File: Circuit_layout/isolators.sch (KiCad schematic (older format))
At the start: 28 parts, among them U16 MCP6004, U17 ACPL-C870, U18 ACPL-C870

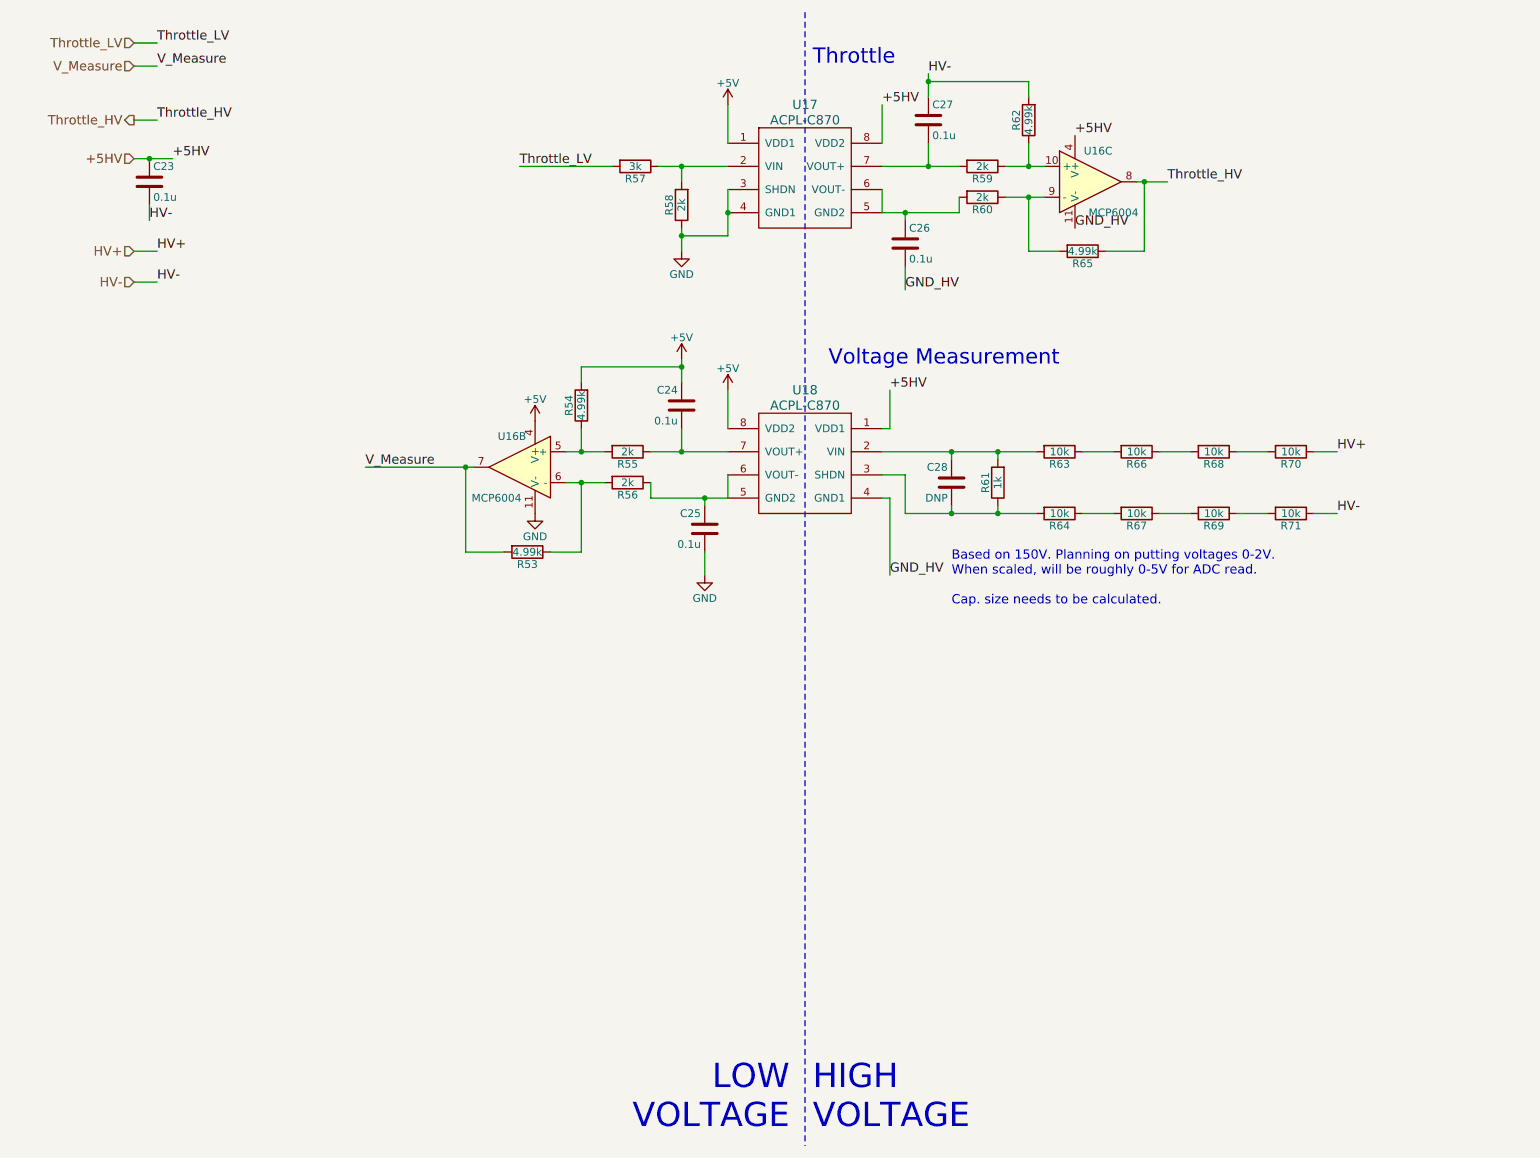
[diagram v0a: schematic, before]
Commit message: finished adding footprints/info to all parts that I can
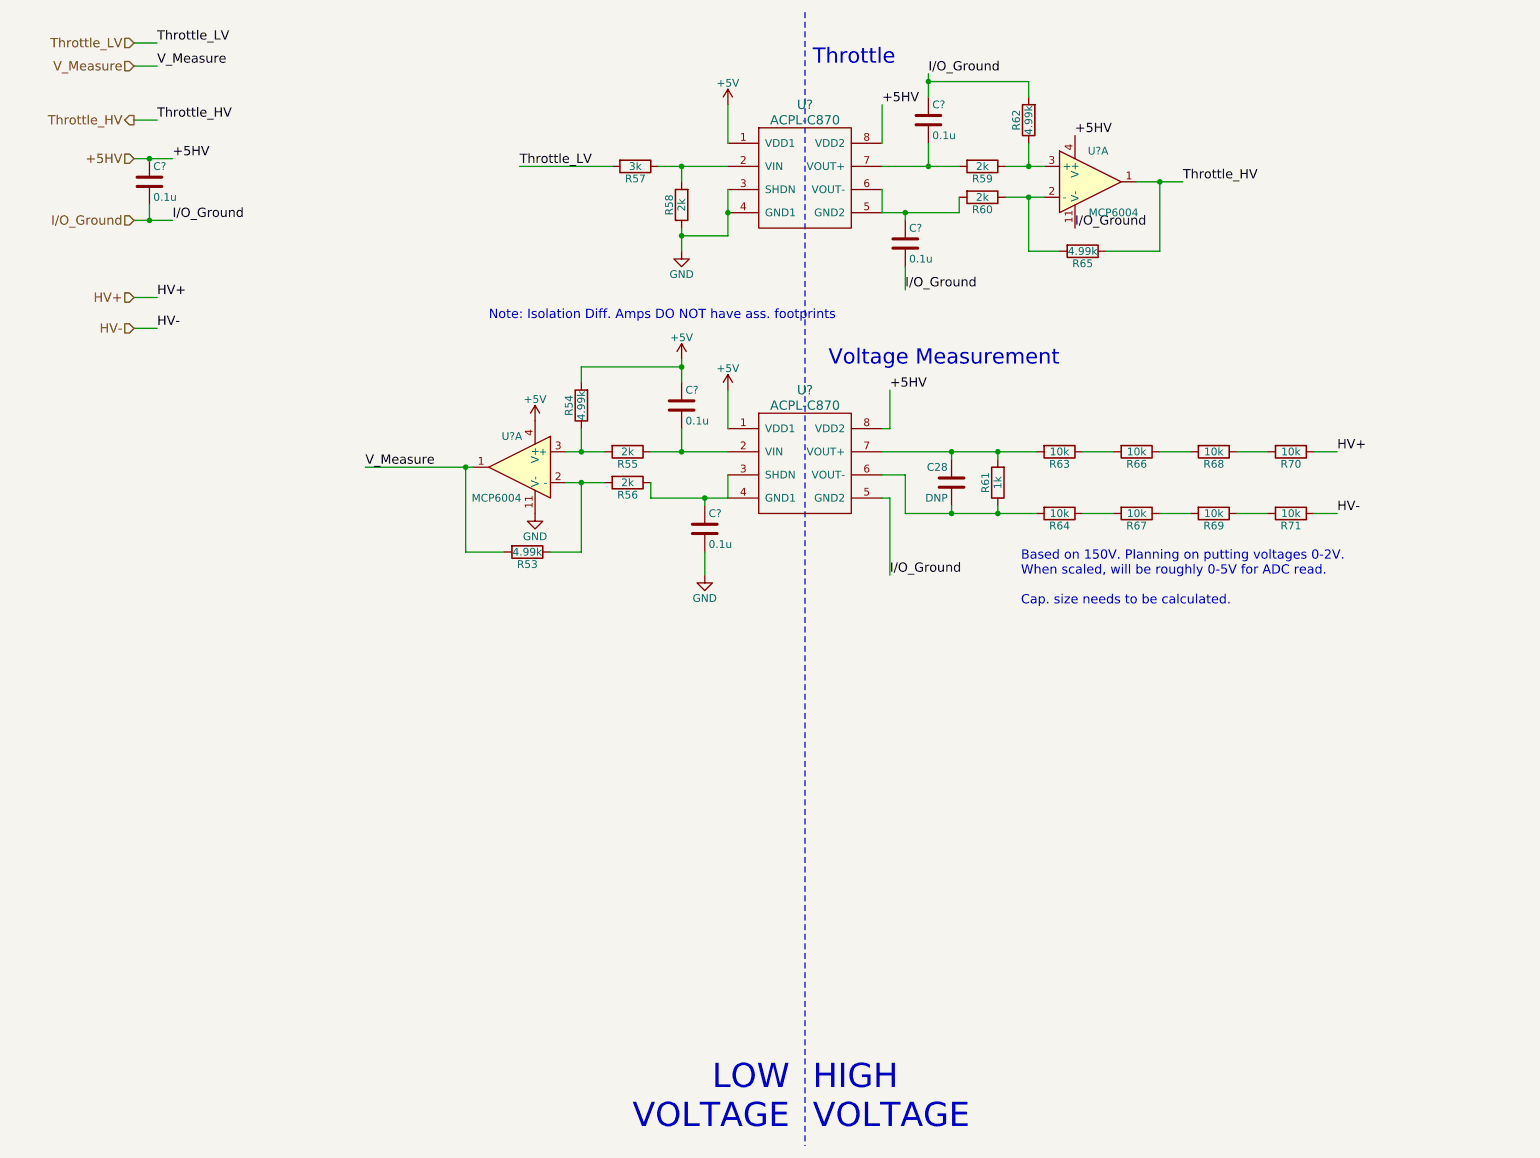
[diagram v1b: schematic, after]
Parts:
- removed C23, C24, C25, C26, C27: 0.1u, symbol C
- removed U16: MCP6004, symbol MCP6004
- removed U17, U18: ACPL-C870, symbol ACPL-C870
- added C? (x5): 0.1u, Capacitors_SMD:C_0805_HandSoldering, symbol C
- added U? (x2): ACPL-C870, symbol ACPL-C870
- added U? (x2): MCP6004, Housings_SOIC:SOIC-14_3.9x8.7mm_Pitch1.27mm, symbol MCP6004
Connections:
- net +5HV: now also C?.1, U?.4 (V+), U?.8 (VDD2), U?.8 (VDD2)
- net +5V: now also C?.1, U?.1 (VDD1), U?.1 (VDD1), U?.4 (V+)
- net GND: now also C?.2, U?.11 (V-), U?.3 (SHDN), U?.4 (GND1)
- net HV-: no longer R62.2
- net Throttle_HV: now also U?.1
- net V_Measure: now also U?.1
- net at R57.1, R58.2: now also U?.2 (VIN)
- net at R60.2: now also C?.1, U?.5 (GND2), U?.6 (VOUT-)
- net at R59.2: now also C?.2, U?.7 (VOUT+)
- net at R59.1, R62.1: now also U?.3 (+)
- net at R60.1, R65.2: now also U?.2 (-)
- net at C28.1, R61.2, R63.2: now also U?.7 (VOUT+)
- net at C28.2, R61.1, R64.2: now also U?.6 (VOUT-)
- net at R56.1: now also C?.1, U?.3 (SHDN), U?.4 (GND1)
- net at R55.1: now also C?.2, U?.2 (VIN)
- net at R54.1, R55.2: now also U?.3 (+)
- net at R53.1, R56.2: now also U?.2 (-)
- new net I/O_Ground: C?.1, C?.2, C?.2, R62.2, U?.11 (V-), U?.5 (GND2)
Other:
- note added: "Note: Isolation Diff. Amps DO NOT have ass. footprints"

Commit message: took notes w/ greg
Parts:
- gave numbers to parts that had none: 8
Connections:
- net Throttle_HV: now also U17.14; no longer U17.1
- net V_Measure: now also U17.8; no longer U17.1
- net at R60.1, R65.2: now also U17.13 (-); no longer U17.2 (-)
- net at R59.1, R62.1: now also U17.12 (+); no longer U17.3 (+)
- net at R53.1, R56.2: now also U17.9 (-); no longer U17.2 (-)
- net at R54.1, R55.2: now also U17.10 (+); no longer U17.3 (+)
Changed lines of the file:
@@
 	3250 3950 3500 3950
 $Comp
-L +5V #PWR088
+L +5V #PWR087
 U 1 1 58B246C4
 P 4650 2700
-F 0 "#PWR088" H 4650 2550 50  0001 C CNN
+F 0 "#PWR087" H 4650 2550 50  0001 C CNN
 F 1 "+5V" H 4650 2840 50  0000 C CNN
 F 2 "" H 4650 2700 50  0000 C CNN
@@
 $EndComp
 $Comp
-L +5V #PWR089
+L +5V #PWR088
 U 1 1 58B24710
 P 4950 2900
-F 0 "#PWR089" H 4950 2750 50  0001 C CNN
+F 0 "#PWR088" H 4950 2750 50  0001 C CNN
 F 1 "+5V" H 4950 3040 50  0000 C CNN
 F 2 "" H 4950 2900 50  0000 C CNN
@@
 $EndComp
 $Comp
-L +5V #PWR090
+L +5V #PWR089
 U 1 1 58B2475C
 P 3700 3100
-F 0 "#PWR090" H 3700 2950 50  0001 C CNN
+F 0 "#PWR089" H 3700 2950 50  0001 C CNN
 F 1 "+5V" H 3700 3240 50  0000 C CNN
 F 2 "" H 3700 3100 50  0000 C CNN
@@
 $EndComp
 $Comp
-L GND #PWR091
+L GND #PWR090
 U 1 1 58B247A8
 P 3700 3700
-F 0 "#PWR091" H 3700 3450 50  0001 C CNN
+F 0 "#PWR090" H 3700 3450 50  0001 C CNN
 F 1 "GND" H 3700 3550 50  0000 C CNN
 F 2 "" H 3700 3700 50  0000 C CNN
@@
 $EndComp
 $Comp
-L GND #PWR092
+L GND #PWR091
 U 1 1 58B2480E
 P 4800 4100
-F 0 "#PWR092" H 4800 3850 50  0001 C CNN
+F 0 "#PWR091" H 4800 3850 50  0001 C CNN
 F 1 "GND" H 4800 3950 50  0000 C CNN
 F 2 "" H 4800 4100 50  0000 C CNN
@@
 	4950 1900 4650 1900
 $Comp
-L GND #PWR093
+L GND #PWR092
 U 1 1 58B25770
 P 4650 2000
-F 0 "#PWR093" H 4650 1750 50  0001 C CNN
+F 0 "#PWR092" H 4650 1750 50  0001 C CNN
 F 1 "GND" H 4650 1850 50  0000 C CNN
 F 2 "" H 4650 2000 50  0000 C CNN
@@
 $EndComp
 $Comp
-L +5V #PWR094
+L +5V #PWR093
 U 1 1 58B257CF
 P 4950 1050
-F 0 "#PWR094" H 4950 900 50  0001 C CNN
+F 0 "#PWR093" H 4950 900 50  0001 C CNN
 F 1 "+5V" H 4950 1190 50  0000 C CNN
 F 2 "" H 4950 1050 50  0000 C CNN
@@
 $EndComp
 $Comp
-L C C?
+L C C25
 U 1 1 58B44F65
 P 1200 1550
-F 0 "C?" H 1225 1650 50  0000 L CNN
+F 0 "C25" H 1225 1650 50  0000 L CNN
 F 1 "0.1u" H 1225 1450 50  0000 L CNN
 F 2 "Capacitors_SMD:C_0805_HandSoldering" H 1238 1400 50  0001 C CNN
@@
 $EndComp
 $Comp
-L ACPL-C870 U?
+L ACPL-C870 U19
 U 1 1 58B45431
 P 5450 1250
-F 0 "U?" H 5450 1450 60  0000 C CNN
+F 0 "U19" H 5450 1450 60  0000 C CNN
 F 1 "ACPL-C870" H 5450 1350 60  0000 C CNN
 F 2 "" H 5450 1450 60  0000 C CNN
@@
 Note: Isolation Diff. Amps DO NOT have ass. footprints
 $Comp
-L ACPL-C870 U?
+L ACPL-C870 U20
 U 1 1 58B35F2C
 P 5450 3100
-F 0 "U?" H 5450 3300 60  0000 C CNN
+F 0 "U20" H 5450 3300 60  0000 C CNN
 F 1 "ACPL-C870" H 5450 3200 60  0000 C CNN
 F 2 "" H 5450 3300 60  0000 C CNN
@@
 $EndComp
 $Comp
-L C C?
+L C C26
 U 1 1 58B362A1
 P 4650 3000
-F 0 "C?" H 4675 3100 50  0000 L CNN
+F 0 "C26" H 4675 3100 50  0000 L CNN
 F 1 "0.1u" H 4675 2900 50  0000 L CNN
 F 2 "Capacitors_SMD:C_0805_HandSoldering" H 4688 2850 50  0001 C CNN
@@
 $EndComp
 $Comp
-L C C?
+L C C27
 U 1 1 58B36392
 P 4800 3800
-F 0 "C?" H 4825 3900 50  0000 L CNN
+F 0 "C27" H 4825 3900 50  0000 L CNN
 F 1 "0.1u" H 4825 3700 50  0000 L CNN
 F 2 "Capacitors_SMD:C_0805_HandSoldering" H 4838 3650 50  0001 C CNN
@@
 $EndComp
 $Comp
-L C C?
+L C C30
 U 1 1 58B3649B
 P 6250 1150
-F 0 "C?" H 6275 1250 50  0000 L CNN
+F 0 "C30" H 6275 1250 50  0000 L CNN
 F 1 "0.1u" H 6275 1050 50  0000 L CNN
 F 2 "Capacitors_SMD:C_0805_HandSoldering" H 6288 1000 50  0001 C CNN
@@
 $EndComp
 $Comp
-L C C?
+L C C29
 U 1 1 58B36598
 P 6100 1950
-F 0 "C?" H 6125 2050 50  0000 L CNN
+F 0 "C29" H 6125 2050 50  0000 L CNN
 F 1 "0.1u" H 6125 1850 50  0000 L CNN
 F 2 "Capacitors_SMD:C_0805_HandSoldering" H 6138 1800 50  0001 C CNN
@@
 $EndComp
 $Comp
-L MCP6004 U?
-U 1 1 58B3670F
+L MCP6004 U17
+U 4 1 58B3670F
 P 7300 1550
-F 0 "U?" H 7350 1750 50  0000 C CNN
+F 0 "U17" H 7350 1750 50  0000 C CNN
 F 1 "MCP6004" H 7450 1350 50  0000 C CNN
 F 2 "Housings_SOIC:SOIC-14_3.9x8.7mm_Pitch1.27mm" H 7250 1650 50  0001 C CNN
@@
 F 5 "http://www.digikey.com/product-detail/en/microchip-technology/MCP6004T-I-SL/MCP6004T-I-SLCT-ND/5013527" H 7300 1550 60  0001 C CNN "URL"
 F 6 "MCP6004T-I/SL" H 7300 1550 60  0001 C CNN "Man P/N"
-	1    7300 1550
-	1    0    0    -1
-$EndComp
-$Comp
-L MCP6004 U?
-U 1 1 58B367EC
+	4    7300 1550
+	1    0    0    -1
+$EndComp
+$Comp
+L MCP6004 U17
+U 3 1 58B367EC
 P 3600 3400
-F 0 "U?" H 3650 3600 50  0000 C CNN
+F 0 "U17" H 3650 3600 50  0000 C CNN
 F 1 "MCP6004" H 3750 3200 50  0000 C CNN
 F 2 "Housings_SOIC:SOIC-14_3.9x8.7mm_Pitch1.27mm" H 3550 3500 50  0001 C CNN
@@
 F 5 "http://www.digikey.com/product-detail/en/microchip-technology/MCP6004T-I-SL/MCP6004T-I-SLCT-ND/5013527" H 3600 3400 60  0001 C CNN "URL"
 F 6 "MCP6004T-I/SL" H 3600 3400 60  0001 C CNN "Man P/N"
-	1    3600 3400
+	3    3600 3400
 	-1   0    0    -1
 $EndComp

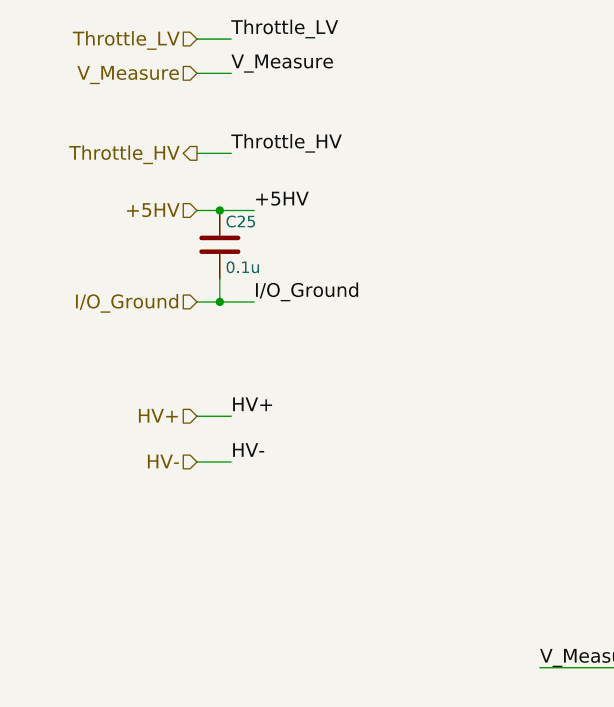
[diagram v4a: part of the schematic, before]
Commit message: got rid of some warnings with nets.
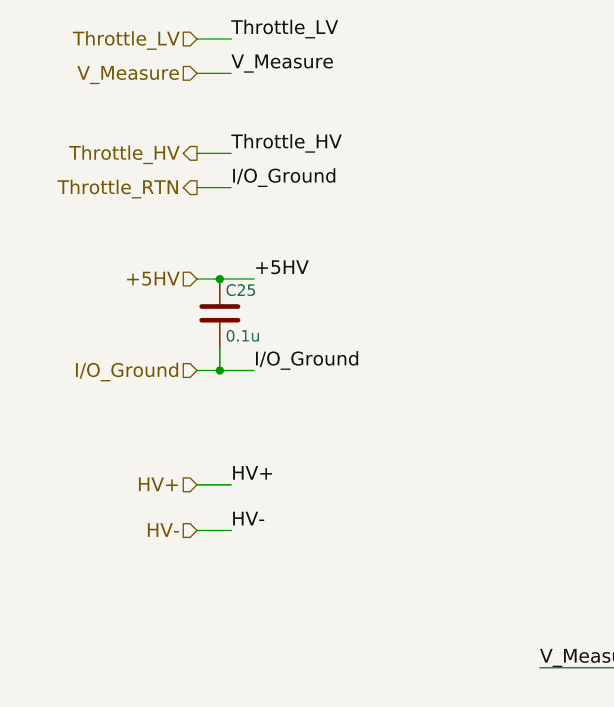
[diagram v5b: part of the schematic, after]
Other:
- moved on the sheet: C25
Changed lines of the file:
@@
 Text HLabel 1100 650  0    60   Input ~ 0
 Throttle_LV
-Text HLabel 1100 1400 0    60   Input ~ 0
+Text HLabel 1100 1700 0    60   Input ~ 0
 +5HV
-Text HLabel 1100 2300 0    60   Input ~ 0
+Text HLabel 1100 2600 0    60   Input ~ 0
 HV+
-Text HLabel 1100 2500 0    60   Input ~ 0
+Text HLabel 1100 2800 0    60   Input ~ 0
 HV-
 Text HLabel 1100 1150 0    60   Output ~ 0
@@
 	3250 3950 3500 3950
 $Comp
-L +5V #PWR087
+L +5V #PWR089
 U 1 1 58B246C4
 P 4650 2700
-F 0 "#PWR087" H 4650 2550 50  0001 C CNN
+F 0 "#PWR089" H 4650 2550 50  0001 C CNN
 F 1 "+5V" H 4650 2840 50  0000 C CNN
 F 2 "" H 4650 2700 50  0000 C CNN
@@
 $EndComp
 $Comp
-L +5V #PWR088
+L +5V #PWR090
 U 1 1 58B24710
 P 4950 2900
-F 0 "#PWR088" H 4950 2750 50  0001 C CNN
+F 0 "#PWR090" H 4950 2750 50  0001 C CNN
 F 1 "+5V" H 4950 3040 50  0000 C CNN
 F 2 "" H 4950 2900 50  0000 C CNN
@@
 $EndComp
 $Comp
-L +5V #PWR089
+L +5V #PWR091
 U 1 1 58B2475C
 P 3700 3100
-F 0 "#PWR089" H 3700 2950 50  0001 C CNN
+F 0 "#PWR091" H 3700 2950 50  0001 C CNN
 F 1 "+5V" H 3700 3240 50  0000 C CNN
 F 2 "" H 3700 3100 50  0000 C CNN
@@
 $EndComp
 $Comp
-L GND #PWR090
+L GND #PWR092
 U 1 1 58B247A8
 P 3700 3700
-F 0 "#PWR090" H 3700 3450 50  0001 C CNN
+F 0 "#PWR092" H 3700 3450 50  0001 C CNN
 F 1 "GND" H 3700 3550 50  0000 C CNN
 F 2 "" H 3700 3700 50  0000 C CNN
@@
 $EndComp
 $Comp
-L GND #PWR091
+L GND #PWR093
 U 1 1 58B2480E
 P 4800 4100
-F 0 "#PWR091" H 4800 3850 50  0001 C CNN
+F 0 "#PWR093" H 4800 3850 50  0001 C CNN
 F 1 "GND" H 4800 3950 50  0000 C CNN
 F 2 "" H 4800 4100 50  0000 C CNN
@@
 	4950 1900 4650 1900
 $Comp
-L GND #PWR092
+L GND #PWR094
 U 1 1 58B25770
 P 4650 2000
-F 0 "#PWR092" H 4650 1750 50  0001 C CNN
+F 0 "#PWR094" H 4650 1750 50  0001 C CNN
 F 1 "GND" H 4650 1850 50  0000 C CNN
 F 2 "" H 4650 2000 50  0000 C CNN
@@
 $EndComp
 $Comp
-L +5V #PWR093
+L +5V #PWR095
 U 1 1 58B257CF
 P 4950 1050
-F 0 "#PWR093" H 4950 900 50  0001 C CNN
+F 0 "#PWR095" H 4950 900 50  0001 C CNN
 F 1 "+5V" H 4950 1190 50  0000 C CNN
 F 2 "" H 4950 1050 50  0000 C CNN
@@
 $EndComp
 Wire Wire Line
-	1100 2500 1250 2500
-Wire Wire Line
-	1100 2300 1250 2300
+	1100 2800 1250 2800
+Wire Wire Line
+	1100 2600 1250 2600
 Wire Wire Line
 	1100 1150 1250 1150
@@
 Text Label 1250 1150 0    60   ~ 0
 Throttle_HV
-Text Label 1350 1400 0    60   ~ 0
+Text Label 1350 1700 0    60   ~ 0
 +5HV
-Text Label 1250 2300 0    60   ~ 0
+Text Label 1250 2600 0    60   ~ 0
 HV+
-Text Label 1250 2500 0    60   ~ 0
+Text Label 1250 2800 0    60   ~ 0
 HV-
 Wire Wire Line
-	1100 1400 1350 1400
-Connection ~ 1200 1400
-Wire Wire Line
-	1200 1700 1200 1800
+	1100 1700 1350 1700
+Connection ~ 1200 1700
+Wire Wire Line
+	1200 2000 1200 2100
 $Comp
 L R R64
@@
 L C C25
 U 1 1 58B44F65
-P 1200 1550
-F 0 "C25" H 1225 1650 50  0000 L CNN
-F 1 "0.1u" H 1225 1450 50  0000 L CNN
-F 2 "Capacitors_SMD:C_0805_HandSoldering" H 1238 1400 50  0001 C CNN
-F 3 "http://www.kemet.com/Lists/ProductCatalog/Attachments/53/KEM_C1002_X7R_SMD.pdf" H 1200 1550 50  0001 C CNN
-F 4 "399-1168-1-ND" H 1200 1550 60  0001 C CNN "Digikey P/N"
-F 5 "http://www.digikey.com/product-detail/en/kemet/C0805C104K3RACTU/399-1168-1-ND/411443" H 1200 1550 60  0001 C CNN "URL"
-F 6 "C0805C104K3RACTU" H 1200 1550 60  0001 C CNN "Man P/N"
-	1    1200 1550
+P 1200 1850
+F 0 "C25" H 1225 1950 50  0000 L CNN
+F 1 "0.1u" H 1225 1750 50  0000 L CNN
+F 2 "Capacitors_SMD:C_0805_HandSoldering" H 1238 1700 50  0001 C CNN
+F 3 "http://www.kemet.com/Lists/ProductCatalog/Attachments/53/KEM_C1002_X7R_SMD.pdf" H 1200 1850 50  0001 C CNN
+F 4 "399-1168-1-ND" H 1200 1850 60  0001 C CNN "Digikey P/N"
+F 5 "http://www.digikey.com/product-detail/en/kemet/C0805C104K3RACTU/399-1168-1-ND/411443" H 1200 1850 60  0001 C CNN "URL"
+F 6 "C0805C104K3RACTU" H 1200 1850 60  0001 C CNN "Man P/N"
+	1    1200 1850
 	1    0    0    -1
 $EndComp
@@
 	-1   0    0    -1
 $EndComp
-Text Label 1350 1800 0    60   ~ 0
+Text Label 1350 2100 0    60   ~ 0
 I/O_Ground
 Text Label 6250 850  0    60   ~ 0
 I/O_Ground
-Connection ~ 1200 1800
-Wire Wire Line
-	1100 1800 1350 1800
-Text HLabel 1100 1800 0    60   Input ~ 0
+Connection ~ 1200 2100
+Wire Wire Line
+	1100 2100 1350 2100
+Text HLabel 1100 2100 0    60   Input ~ 0
+I/O_Ground
+Text HLabel 1100 1300 0    60   Output ~ 0
+Throttle_RTN
+Wire Wire Line
+	1100 1300 1250 1300
+Text Label 1250 1300 0    60   ~ 0
 I/O_Ground
 $EndSCHEMATC
